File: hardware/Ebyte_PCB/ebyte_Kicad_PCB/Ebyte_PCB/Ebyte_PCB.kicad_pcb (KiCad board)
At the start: 2 copper layers, 30 parts, among them Q1 NPN, Q2 PMOS, U1 DF11, U2 LT8612IUDE, U3 E32-400M33S SX1278, U4 MIC69303RT, U5 CONMMCX001, U6 SN74LVC1G08DBVR

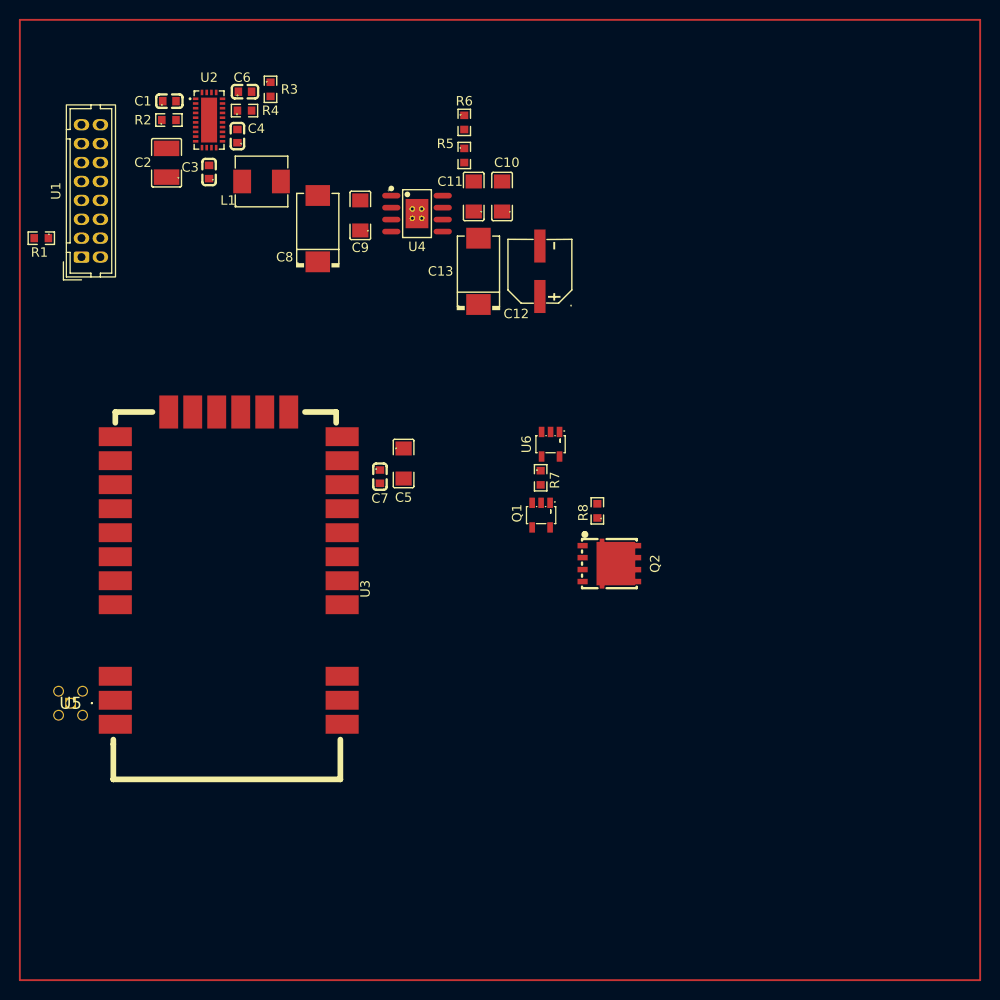
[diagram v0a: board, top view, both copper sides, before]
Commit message: Layout v2
added courtyards, grouped components per datasheet specs. unsure of load switch placement. still figuring out ldo 150u cap.
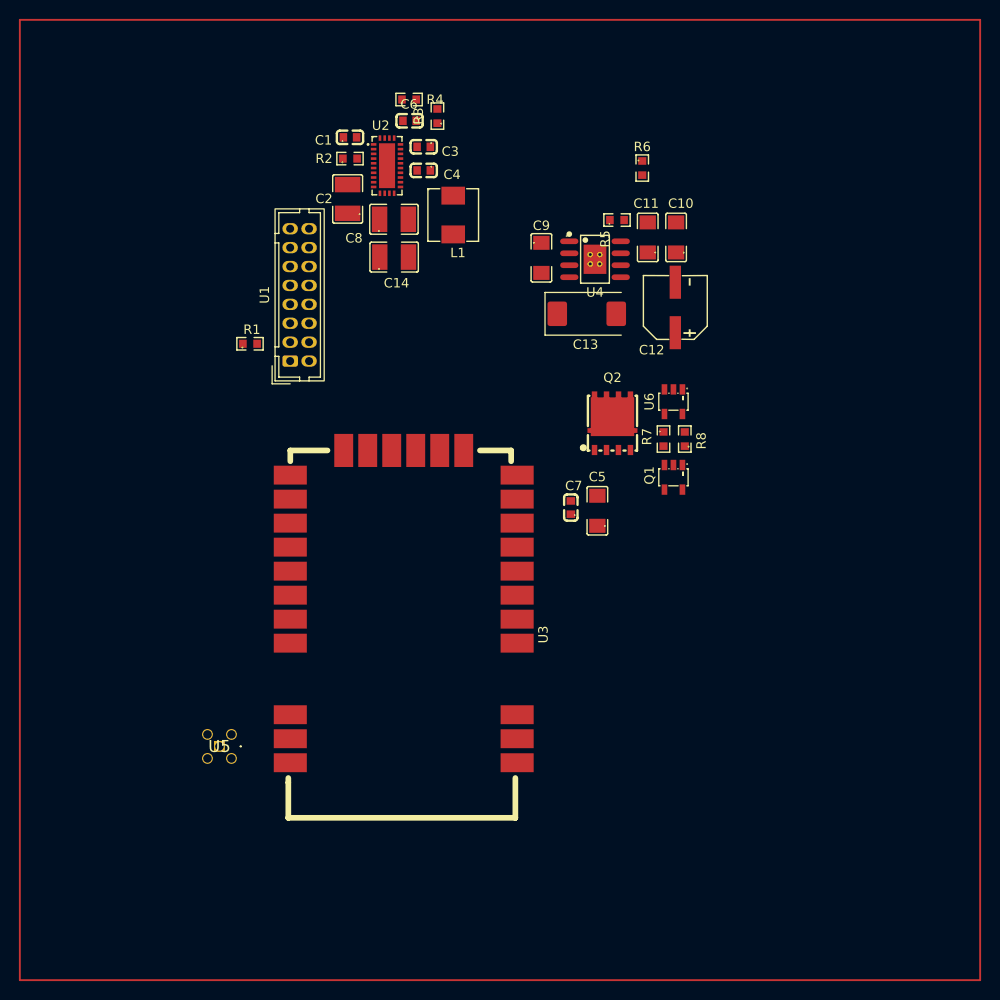
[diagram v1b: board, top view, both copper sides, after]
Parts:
- added C14: 47u, ebyte_footprints:C1210, F.Cu at (65.0, 50.5)
- C13: footprint ebyte_footprints:CAP-SMD_L7.3-W4.3-R-RD -> Capacitor_Tantalum_SMD:CP_EIA-7343-31_Kemet-D
- C8: value 100u -> 47u; footprint ebyte_footprints:CAP-SMD_L7.3-W4.3-R-RD -> ebyte_footprints:C1210
- moved R1 24.7 mm to (49.8, 59.7), turned to 0 degrees
- moved U1 24.7 mm to (54.0, 61.5)
- moved C3 22.9 mm to (68.1, 38.5), turned to 180 degrees
- moved C5 21.1 mm to (86.5, 77.3), turned to 90 degrees
- moved C7 20.8 mm to (84.0, 77.0), turned to 90 degrees
- moved L1 20.6 mm to (71.2, 46.0), turned to -90 degrees
- moved C4 20.0 mm to (68.1, 41.0), turned to 180 degrees
- moved C9 19.7 mm to (80.6, 50.6), turned to -90 degrees
- moved R2 19.6 mm to (60.3, 40.1)
- moved C1 19.6 mm to (60.3, 38.1)
- moved C2 19.5 mm to (60.1, 44.4)
- moved R6 19.4 mm to (91.2, 41.1)
- moved U2 19.4 mm to (64.2, 40.8)
- moved U3 19.4 mm to (54.3, 71.7)
- moved U4 19.4 mm to (86.2, 50.7)
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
